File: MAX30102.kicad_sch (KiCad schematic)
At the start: 7 parts, among them U4 MAX30102, U7 AZ1117-1.8

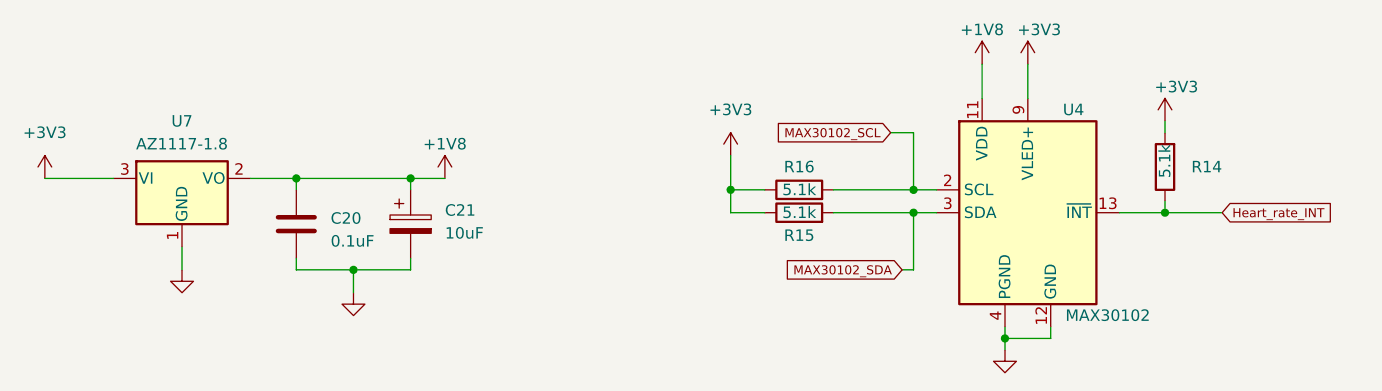
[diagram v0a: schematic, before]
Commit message: assigned footprints and checked the schematic
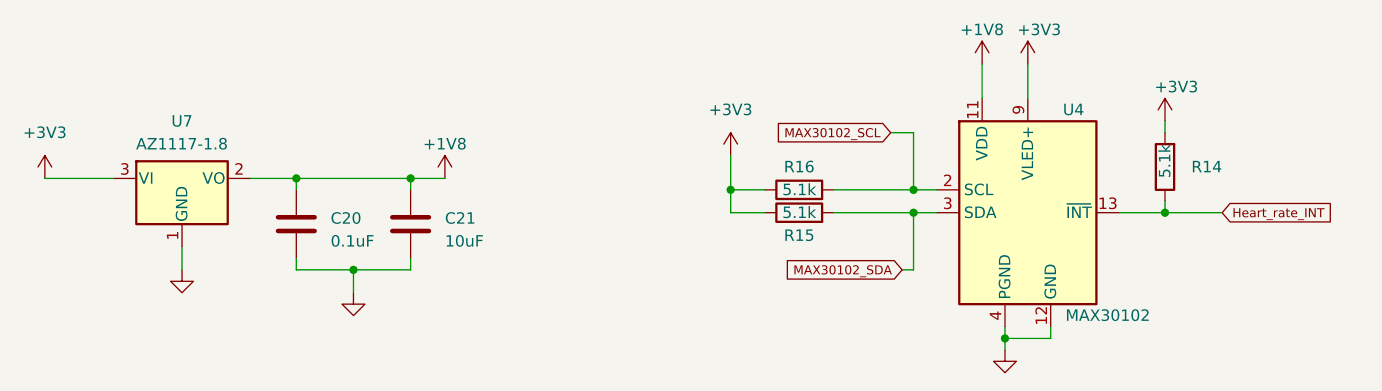
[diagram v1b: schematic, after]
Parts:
- removed C21: 10uF, symbol Device:C_Polarized
- added C21: 10uF, Capacitor_SMD:C_0402_1005Metric_Pad0.74x0.62mm_HandSolder, symbol Device:C
- C20: footprint (none) -> Capacitor_SMD:C_0402_1005Metric_Pad0.74x0.62mm_HandSolder
- R14, R15, R16: footprint (none) -> Resistor_SMD:R_0402_1005Metric_Pad0.72x0.64mm_HandSolder
- U7: footprint (none) -> Package_TO_SOT_SMD:SOT-89-3
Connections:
- net +1V8: now also C21.1
- net GND: now also C21.2
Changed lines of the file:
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@@
       (effects (font (size 1.27 1.27)))
     )
-    (property "Footprint" "" (at 100.33 96.52 0)
+    (property "Footprint" "Package_TO_SOT_SMD:SOT-89-3" (at 100.33 96.52 0)
       (effects (font (size 1.27 1.27) italic) hide)
     )
@@
       (effects (font (size 1.27 1.27)) (justify left))
     )
-    (property "Footprint" "" (at 113.9952 111.76 0)
+    (property "Footprint" "Capacitor_SMD:C_0402_1005Metric_Pad0.74x0.62mm_HandSolder" (at 113.9952 111.76 0)
       (effects (font (size 1.27 1.27)) hide)
     )
@@
       (effects (font (size 1.27 1.27)))
     )
-    (property "Footprint" "" (at 168.91 108.458 90)
+    (property "Footprint" "Resistor_SMD:R_0402_1005Metric_Pad0.72x0.64mm_HandSolder" (at 168.91 108.458 90)
       (effects (font (size 1.27 1.27)) hide)
     )
@@
       (effects (font (size 1.27 1.27)))
     )
-    (property "Footprint" "" (at 168.91 105.918 90)
+    (property "Footprint" "Resistor_SMD:R_0402_1005Metric_Pad0.72x0.64mm_HandSolder" (at 168.91 105.918 90)
       (effects (font (size 1.27 1.27)) hide)
     )
@@
       (effects (font (size 1.27 1.27)) (justify left))
     )
-    (property "Footprint" "" (at 211.328 101.6 90)
+    (property "Footprint" "Resistor_SMD:R_0402_1005Metric_Pad0.72x0.64mm_HandSolder" (at 211.328 101.6 90)
       (effects (font (size 1.27 1.27)) hide)
     )
@@
     )
   )
-  (symbol (lib_id "Device:C_Polarized") (at 125.73 107.95 0) (unit 1)
-    (in_bom yes) (on_board yes) (dnp no) (fields_autoplaced)
-    (property "Reference" "C21" (at 129.54 106.426 0)
-      (effects (font (size 1.27 1.27)) (justify left))
-    )
-    (property "Value" "10uF" (at 129.54 108.966 0)
-      (effects (font (size 1.27 1.27)) (justify left))
-    )
-    (property "Footprint" "" (at 126.6952 111.76 0)
-      (effects (font (size 1.27 1.27)) hide)
-    )
+  (symbol (lib_id "Device:C") (at 125.73 107.95 0) (unit 1)
+    (in_bom yes) (on_board yes) (dnp no) (fields_autoplaced)
+    (property "Reference" "C21" (at 129.54 107.315 0)
+      (effects (font (size 1.27 1.27)) (justify left))
+    )
+    (property "Value" "10uF" (at 129.54 109.855 0)
+      (effects (font (size 1.27 1.27)) (justify left))
+    )
+    (property "Footprint" "Capacitor_SMD:C_0402_1005Metric_Pad0.74x0.62mm_HandSolder" (at 126.6952 111.76 0)
+      (effects (font (size 1.27 1.27)) hide)
+    )

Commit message: Final Design
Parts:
- removed U7: AZ1117-1.8, Package_TO_SOT_SMD:SOT-89-3, symbol Regulator_Linear:AZ1117-1.8
- added U9: AP2127K-1.8, Package_TO_SOT_SMD:SOT-23-5, symbol Regulator_Linear:AP2127K-1.8
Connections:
- net +1V8: now also U9.5 (VOUT)
- net +3V3: now also U9.1 (VIN), U9.3 (EN)
- net GND: now also U9.2 (GND)
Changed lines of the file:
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@@
   (junction (at 181.61 106.68) (diameter 0) (color 0 0 0 0)
   )
+  (junction (at 91.44 102.87) (diameter 0) (color 0 0 0 0)
+  )
   (junction (at 181.61 104.14) (diameter 0) (color 0 0 0 0)
   )
   (junction (at 125.73 102.87) (diameter 0) (color 0 0 0 0)
   )
+  (wire (pts (xy 91.44 105.41) (xy 91.44 102.87))
+    (stroke (width 0) (type default))
+  )
   (wire (pts (xy 181.61 113.03) (xy 181.61 106.68))
     (stroke (width 0) (type default))
@@
     (stroke (width 0) (type default))
   )
-  (wire (pts (xy 85.09 102.87) (xy 92.71 102.87))
+  (wire (pts (xy 92.71 105.41) (xy 91.44 105.41))
+    (stroke (width 0) (type default))
+  )
+  (wire (pts (xy 85.09 102.87) (xy 91.44 102.87))
     (stroke (width 0) (type default))
   )
@@
     (stroke (width 0) (type default))
   )
-  (wire (pts (xy 100.33 113.03) (xy 100.33 110.49))
-    (stroke (width 0) (type default))
-  )
   (wire (pts (xy 129.54 102.87) (xy 125.73 102.87))
     (stroke (width 0) (type default))
@@
     (stroke (width 0) (type default))
   )
+  (wire (pts (xy 91.44 102.87) (xy 92.71 102.87))
+    (stroke (width 0) (type default))
+  )
   (wire (pts (xy 113.03 104.14) (xy 113.03 102.87))
     (stroke (width 0) (type default))
@@
   )
   (wire (pts (xy 209.55 106.68) (xy 215.9 106.68))
+    (stroke (width 0) (type default))
+  )
+  (wire (pts (xy 100.33 113.03) (xy 100.33 115.57))
     (stroke (width 0) (type default))
   )
@@
     )
   )
-  (symbol (lib_id "Regulator_Linear:AZ1117-1.8") (at 100.33 102.87 0) (unit 1)
-    (in_bom yes) (on_board yes) (dnp no) (fields_autoplaced)
-    (property "Reference" "U7" (at 100.33 96.52 0)
-      (effects (font (size 1.27 1.27)))
-    )
-    (property "Value" "AZ1117-1.8" (at 100.33 99.06 0)
-      (effects (font (size 1.27 1.27)))
-    )
-    (property "Footprint" "Package_TO_SOT_SMD:SOT-89-3" (at 100.33 96.52 0)
-      (effects (font (size 1.27 1.27) italic) hide)
-    )
-    (property "Datasheet" "https://www.diodes.com/assets/Datasheets/AZ1117.pdf" (at 100.33 102.87 0)
-      (effects (font (size 1.27 1.27)) hide)
-    )
-    (pin "1")
-    (pin "2")
-    (pin "3")
-    (instances
-      (project "RP2040_SOS_band"
-        (path "/1d911b84-17e1-4d47-ac8f-a730104b53ed/d354c91b-03e4-4b78-829b-33cd8f15be96"
-          (reference "U7") (unit 1)
-        )
-      )
-    )
-  )
   (symbol (lib_id "Device:C") (at 113.03 107.95 0) (unit 1)
     (in_bom yes) (on_board yes) (dnp no) (fields_autoplaced)
@@
         (path "/1d911b84-17e1-4d47-ac8f-a730104b53ed/d354c91b-03e4-4b78-829b-33cd8f15be96"
           (reference "#PWR041") (unit 1)
+        )
+      )
+    )
+  )
+  (symbol (lib_id "Regulator_Linear:AP2127K-1.8") (at 100.33 105.41 0) (unit 1)
+    (in_bom yes) (on_board yes) (dnp no) (fields_autoplaced)
+    (property "Reference" "U9" (at 100.33 96.52 0)
+      (effects (font (size 1.27 1.27)))
+    )
+    (property "Value" "AP2127K-1.8" (at 100.33 99.06 0)
+      (effects (font (size 1.27 1.27)))
+    )
+    (property "Footprint" "Package_TO_SOT_SMD:SOT-23-5" (at 100.33 97.155 0)
+      (effects (font (size 1.27 1.27)) hide)
+    )
+    (property "Datasheet" "https://www.diodes.com/assets/Datasheets/AP2127.pdf" (at 100.33 102.87 0)
+      (effects (font (size 1.27 1.27)) hide)
+    )
+    (pin "1")
+    (pin "2")
+    (pin "3")
+    (pin "4")
+    (pin "5")
+    (instances
+      (project "RP2040_SOS_band"
+        (path "/1d911b84-17e1-4d47-ac8f-a730104b53ed/892de33d-264e-4bda-a61c-c8174f81e463"
+          (reference "U9") (unit 1)
+        )
+        (path "/1d911b84-17e1-4d47-ac8f-a730104b53ed/d354c91b-03e4-4b78-829b-33cd8f15be96"
+          (reference "U7") (unit 1)
         )
       )
@@
     )
   )
-  (symbol (lib_id "power:GND") (at 100.33 113.03 0) (unit 1)
-    (in_bom yes) (on_board yes) (dnp no) (fields_autoplaced)
-    (property "Reference" "#PWR031" (at 100.33 119.38 0)
-      (effects (font (size 1.27 1.27)) hide)
-    )
-    (property "Value" "GND" (at 100.33 118.11 0)
-      (effects (font (size 1.27 1.27)) hide)
-    )
-    (property "Footprint" "" (at 100.33 113.03 0)
-      (effects (font (size 1.27 1.27)) hide)
-    )
-    (property "Datasheet" "" (at 100.33 113.03 0)
-      (effects (font (size 1.27 1.27)) hide)
-    )
+  (symbol (lib_id "power:GND") (at 100.33 115.57 0) (unit 1)
+    (in_bom yes) (on_board yes) (dnp no) (fields_autoplaced)
+    (property "Reference" "#PWR031" (at 100.33 121.92 0)
+      (effects (font (size 1.27 1.27)) hide)
+    )
+    (property "Value" "GND" (at 100.33 120.65 0)
+      (effects (font (size 1.27 1.27)) hide)
+    )
+    (property "Footprint" "" (at 100.33 115.57 0)
+      (effects (font (size 1.27 1.27)) hide)
+    )
+    (property "Datasheet" "" (at 100.33 115.57 0)
+      (effects (font (size 1.27 1.27)) hide)
+    )
